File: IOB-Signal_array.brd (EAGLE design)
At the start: 104.1 x 106.7 mm, 49 parts

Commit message: Added missing values
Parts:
- C1X11, C1X12, C1X13, C1X14: value (none) -> 0.1uF
- IC1X11, IC1X12, IC1X13, IC1X14: value (none) -> 74HS139A
- R10X11, R10X12, R10X13, R10X14, R6X11, R6X12, R6X13, R6X14, R7X11, R7X12, R7X13, R7X14, R9X11, R9X12, R9X13, R9X14: value (none) -> 1k0
- R4X11, R4X12, R4X13, R4X14, R8X11, R8X12, R8X13, R8X14: value (none) -> 420R
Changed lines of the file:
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@@
 </autorouter>
 <elements>
-<element name="C1X11" library="SPCoast" package="0805-CAP" value="" x="54.61" y="17.526" rot="R270"/>
+<element name="C1X11" library="SPCoast" package="0805-CAP" value="0.1uF" x="54.61" y="17.526" rot="R270"/>
 <element name="CON1X11" library="SPCoast" package="RJ45-NO-SHIELD" value="" x="29.718" y="17.399" rot="R270"/>
 <element name="FID1X11" library="SPCoast" package="FIDUCIAL_1MM" value="" x="41.275" y="10.287"/>
 <element name="FID3X11" library="SPCoast" package="FIDUCIAL_1MM" value="" x="76.835" y="27.305"/>
-<element name="IC1X11" library="SPCoast" package="SO16" value="" x="60.833" y="17.399"/>
-<element name="R4X11" library="SPCoast" package="0805-RES" value="" x="50.8" y="15.494"/>
-<element name="R6X11" library="SPCoast" package="0805-RES" value="" x="46.99" y="14.224"/>
-<element name="R7X11" library="SPCoast" package="0805-RES" value="" x="46.99" y="16.764"/>
-<element name="R8X11" library="SPCoast" package="0805-RES" value="" x="50.8" y="20.574"/>
-<element name="R9X11" library="SPCoast" package="0805-RES" value="" x="46.99" y="19.304"/>
-<element name="R10X11" library="SPCoast" package="0805-RES" value="" x="46.99" y="21.844"/>
+<element name="IC1X11" library="SPCoast" package="SO16" value="74HS139A" x="60.833" y="17.399"/>
+<element name="R4X11" library="SPCoast" package="0805-RES" value="420R" x="50.8" y="15.494"/>
+<element name="R6X11" library="SPCoast" package="0805-RES" value="1k0" x="46.99" y="14.224"/>
+<element name="R7X11" library="SPCoast" package="0805-RES" value="1k0" x="46.99" y="16.764"/>
+<element name="R8X11" library="SPCoast" package="0805-RES" value="420R" x="50.8" y="20.574"/>
+<element name="R9X11" library="SPCoast" package="0805-RES" value="1k0" x="46.99" y="19.304"/>
+<element name="R10X11" library="SPCoast" package="0805-RES" value="1k0" x="46.99" y="21.844"/>
 <element name="U$1X11" library="SPCoast" package="IO4-IOB" value="" x="25.4" y="8.89"/>
-<element name="C1X12" library="SPCoast" package="0805-CAP" value="" x="54.61" y="37.846" rot="R270"/>
+<element name="C1X12" library="SPCoast" package="0805-CAP" value="0.1uF" x="54.61" y="37.846" rot="R270"/>
 <element name="CON1X12" library="SPCoast" package="RJ45-NO-SHIELD" value="" x="29.718" y="37.719" rot="R270"/>
 <element name="FID1X12" library="SPCoast" package="FIDUCIAL_1MM" value="" x="41.275" y="30.607"/>
 <element name="FID3X12" library="SPCoast" package="FIDUCIAL_1MM" value="" x="76.835" y="47.625"/>
-<element name="IC1X12" library="SPCoast" package="SO16" value="" x="60.833" y="37.719"/>
-<element name="R4X12" library="SPCoast" package="0805-RES" value="" x="50.8" y="35.814"/>
-<element name="R6X12" library="SPCoast" package="0805-RES" value="" x="46.99" y="34.544"/>
-<element name="R7X12" library="SPCoast" package="0805-RES" value="" x="46.99" y="37.084"/>
-<element name="R8X12" library="SPCoast" package="0805-RES" value="" x="50.8" y="40.894"/>
-<element name="R9X12" library="SPCoast" package="0805-RES" value="" x="46.99" y="39.624"/>
-<element name="R10X12" library="SPCoast" package="0805-RES" value="" x="46.99" y="42.164"/>
+<element name="IC1X12" library="SPCoast" package="SO16" value="74HS139A" x="60.833" y="37.719"/>
+<element name="R4X12" library="SPCoast" package="0805-RES" value="420R" x="50.8" y="35.814"/>
+<element name="R6X12" library="SPCoast" package="0805-RES" value="1k0" x="46.99" y="34.544"/>
+<element name="R7X12" library="SPCoast" package="0805-RES" value="1k0" x="46.99" y="37.084"/>
+<element name="R8X12" library="SPCoast" package="0805-RES" value="420R" x="50.8" y="40.894"/>
+<element name="R9X12" library="SPCoast" package="0805-RES" value="1k0" x="46.99" y="39.624"/>
+<element name="R10X12" library="SPCoast" package="0805-RES" value="1k0" x="46.99" y="42.164"/>
 <element name="U$1X12" library="SPCoast" package="IO4-IOB" value="" x="25.4" y="29.21"/>
-<element name="C1X13" library="SPCoast" package="0805-CAP" value="" x="54.61" y="58.166" rot="R270"/>
+<element name="C1X13" library="SPCoast" package="0805-CAP" value="0.1uF" x="54.61" y="58.166" rot="R270"/>
 <element name="CON1X13" library="SPCoast" package="RJ45-NO-SHIELD" value="" x="29.718" y="58.039" rot="R270"/>
 <element name="FID1X13" library="SPCoast" package="FIDUCIAL_1MM" value="" x="41.275" y="50.927"/>
 <element name="FID3X13" library="SPCoast" package="FIDUCIAL_1MM" value="" x="76.835" y="67.945"/>
-<element name="IC1X13" library="SPCoast" package="SO16" value="" x="60.833" y="58.039"/>
-<element name="R4X13" library="SPCoast" package="0805-RES" value="" x="50.8" y="56.134"/>
-<element name="R6X13" library="SPCoast" package="0805-RES" value="" x="46.99" y="54.864"/>
-<element name="R7X13" library="SPCoast" package="0805-RES" value="" x="46.99" y="57.404"/>
-<element name="R8X13" library="SPCoast" package="0805-RES" value="" x="50.8" y="61.214"/>
-<element name="R9X13" library="SPCoast" package="0805-RES" value="" x="46.99" y="59.944"/>
-<element name="R10X13" library="SPCoast" package="0805-RES" value="" x="46.99" y="62.484"/>
+<element name="IC1X13" library="SPCoast" package="SO16" value="74HS139A" x="60.833" y="58.039"/>
+<element name="R4X13" library="SPCoast" package="0805-RES" value="420R" x="50.8" y="56.134"/>
+<element name="R6X13" library="SPCoast" package="0805-RES" value="1k0" x="46.99" y="54.864"/>
+<element name="R7X13" library="SPCoast" package="0805-RES" value="1k0" x="46.99" y="57.404"/>
+<element name="R8X13" library="SPCoast" package="0805-RES" value="420R" x="50.8" y="61.214"/>
+<element name="R9X13" library="SPCoast" package="0805-RES" value="1k0" x="46.99" y="59.944"/>
+<element name="R10X13" library="SPCoast" package="0805-RES" value="1k0" x="46.99" y="62.484"/>
 <element name="U$1X13" library="SPCoast" package="IO4-IOB" value="" x="25.4" y="49.53"/>
-<element name="C1X14" library="SPCoast" package="0805-CAP" value="" x="54.61" y="78.486" rot="R270"/>
+<element name="C1X14" library="SPCoast" package="0805-CAP" value="0.1uF" x="54.61" y="78.486" rot="R270"/>
 <element name="CON1X14" library="SPCoast" package="RJ45-NO-SHIELD" value="" x="29.718" y="78.359" rot="R270"/>
 <element name="FID1X14" library="SPCoast" package="FIDUCIAL_1MM" value="" x="41.275" y="71.247"/>
 <element name="FID3X14" library="SPCoast" package="FIDUCIAL_1MM" value="" x="76.835" y="88.265"/>
-<element name="IC1X14" library="SPCoast" package="SO16" value="" x="60.833" y="78.359"/>
-<element name="R4X14" library="SPCoast" package="0805-RES" value="" x="50.8" y="76.454"/>
-<element name="R6X14" library="SPCoast" package="0805-RES" value="" x="46.99" y="75.184"/>
-<element name="R7X14" library="SPCoast" package="0805-RES" value="" x="46.99" y="77.724"/>
-<element name="R8X14" library="SPCoast" package="0805-RES" value="" x="50.8" y="81.534"/>
-<element name="R9X14" library="SPCoast" package="0805-RES" value="" x="46.99" y="80.264"/>
-<element name="R10X14" library="SPCoast" package="0805-RES" value="" x="46.99" y="82.804"/>
+<element name="IC1X14" library="SPCoast" package="SO16" value="74HS139A" x="60.833" y="78.359"/>
+<element name="R4X14" library="SPCoast" package="0805-RES" value="420R" x="50.8" y="76.454"/>
+<element name="R6X14" library="SPCoast" package="0805-RES" value="1k0" x="46.99" y="75.184"/>
+<element name="R7X14" library="SPCoast" package="0805-RES" value="1k0" x="46.99" y="77.724"/>
+<element name="R8X14" library="SPCoast" package="0805-RES" value="420R" x="50.8" y="81.534"/>
+<element name="R9X14" library="SPCoast" package="0805-RES" value="1k0" x="46.99" y="80.264"/>
+<element name="R10X14" library="SPCoast" package="0805-RES" value="1k0" x="46.99" y="82.804"/>
 <element name="U$1X14" library="SPCoast" package="IO4-IOB" value="" x="25.4" y="69.85"/>
 <element name="U$1X1" library="SPCoast" package="BOARD-DINRAIL-3.17IN-H4X-IOB" value="" x="0" y="0"/>

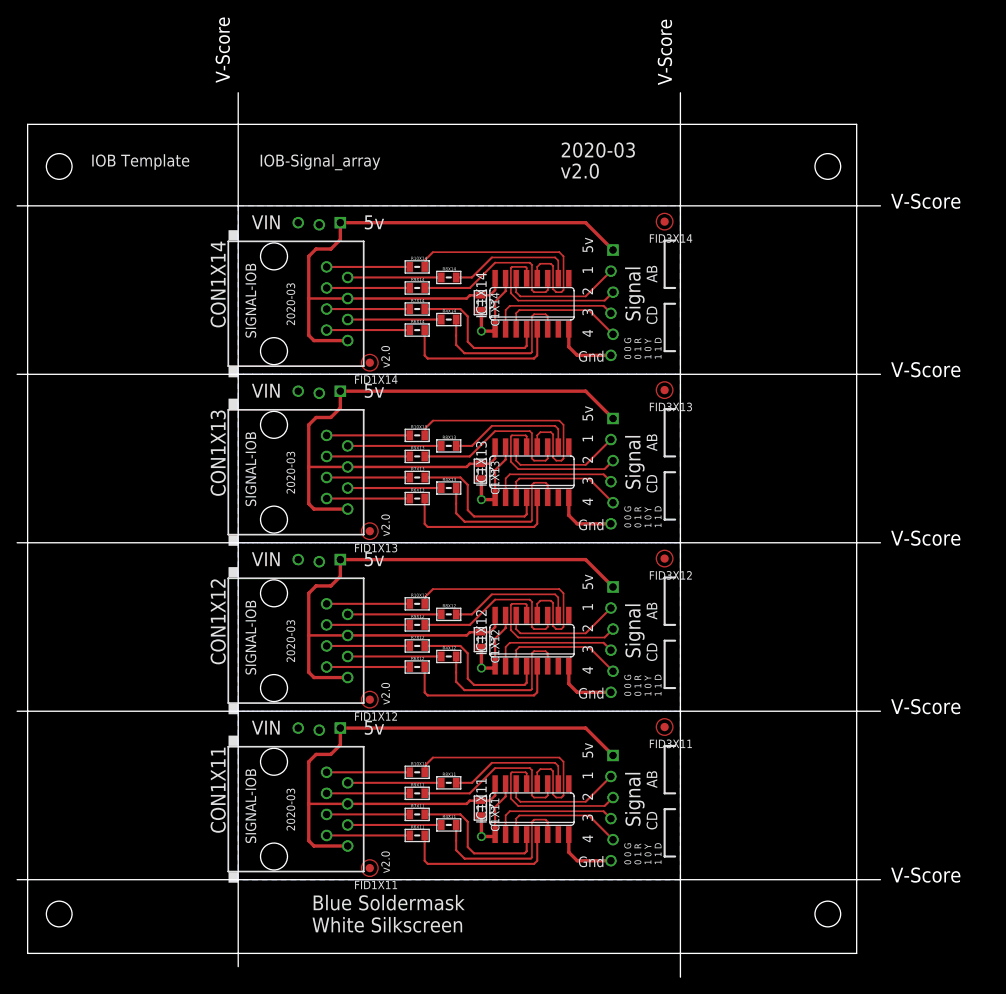
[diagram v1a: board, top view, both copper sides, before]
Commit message: normalized silkscreen layout across IOBs
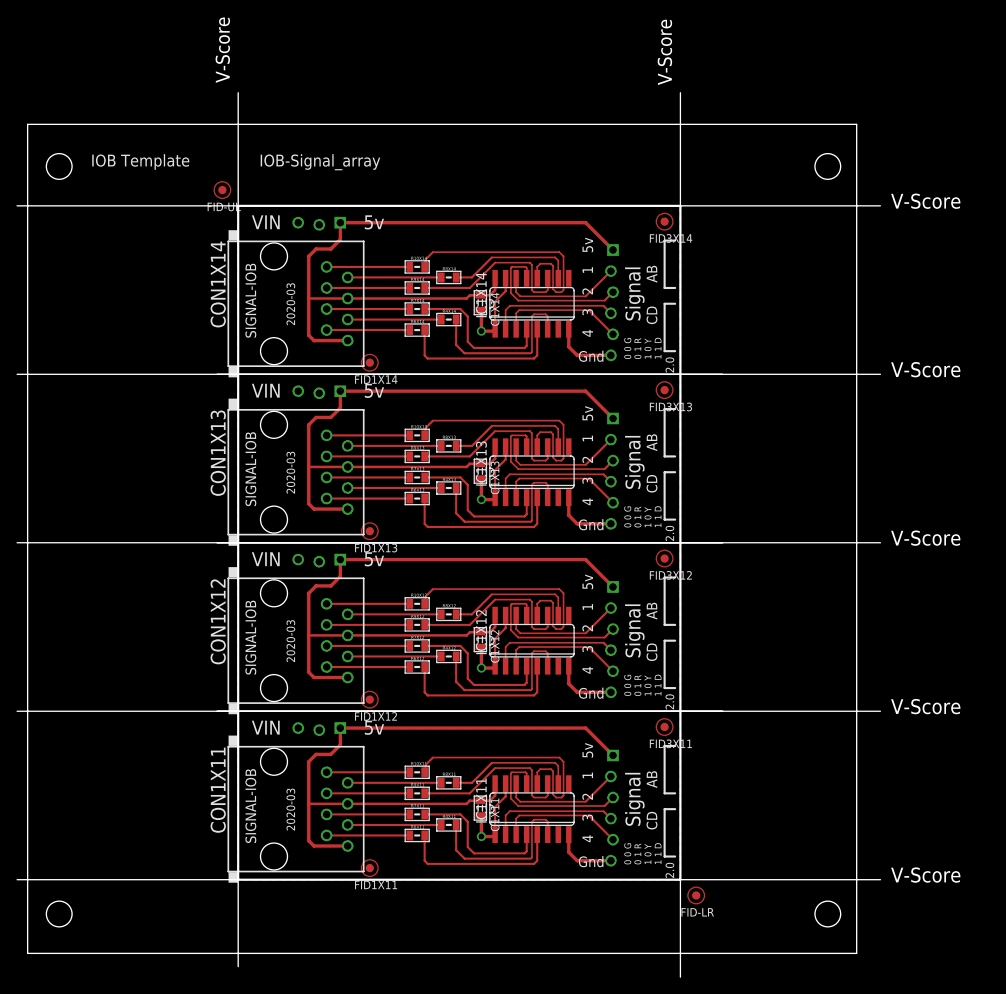
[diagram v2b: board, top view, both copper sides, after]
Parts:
- added FID-LR, FID-UL: FIDUCIAL, SPCoast:FIDUCIAL_1MM
- C1X11, C1X12, C1X13, C1X14: value 0.1uF -> 0.1UF
- CON1X11, CON1X12, CON1X13, CON1X14: value (none) -> RJ45
- FID1X11, FID1X12, FID1X13, FID1X14, FID3X11, FID3X12, FID3X13, FID3X14: value (none) -> FIDUCIAL
- R10X11, R10X12, R10X13, R10X14, R6X11, R6X12, R6X13, R6X14, R7X11, R7X12, R7X13, R7X14, R9X11, R9X12, R9X13, R9X14: value 1k0 -> 1K0
- U$1X11, U$1X12, U$1X13, U$1X14: value (none) -> CONNECTOR-IO4-IOBBARE
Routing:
- added copper zone on layer 1, net VCCX11
- added copper zone on layer 1, net VCCX12
- added copper zone on layer 1, net VCCX13
- added copper zone on layer 1, net VCCX14
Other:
- board text added: "2.0"
- board text added: "Blue Header"
- board text removed: "v2.0"

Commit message: bottom silk alignment
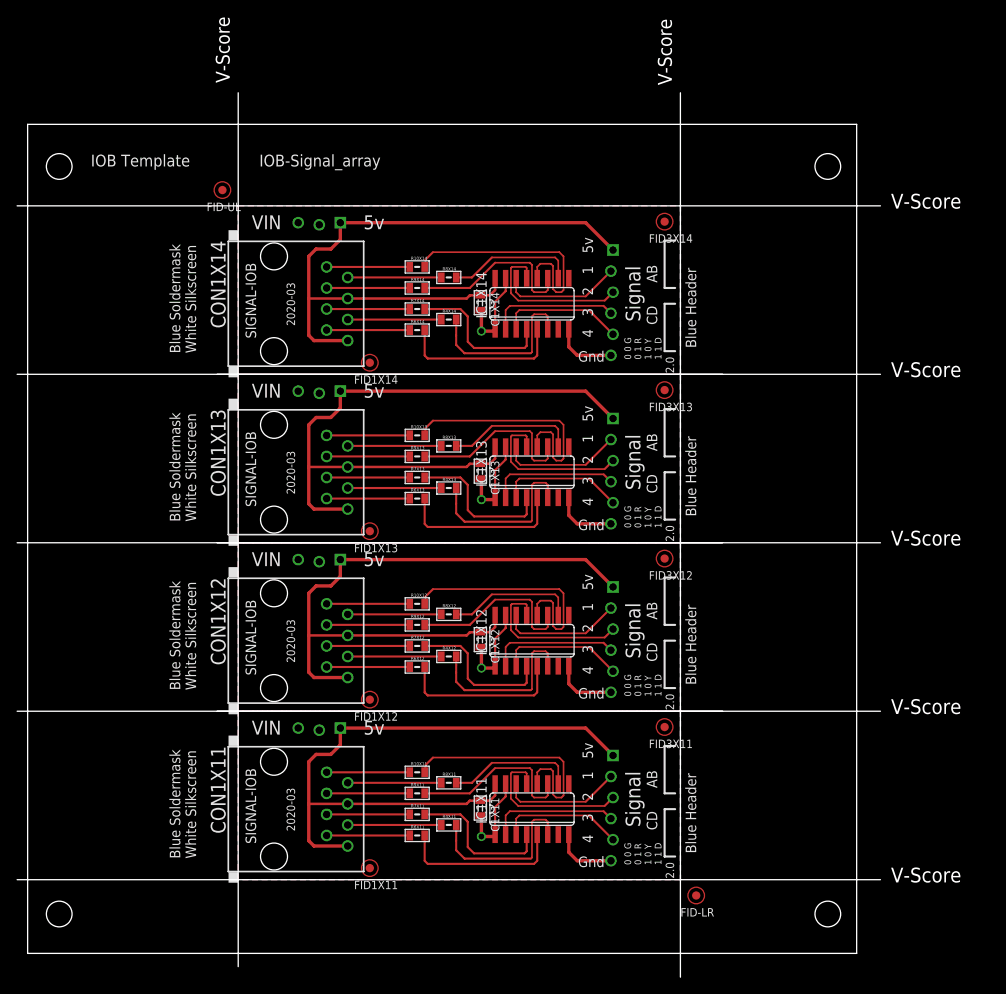
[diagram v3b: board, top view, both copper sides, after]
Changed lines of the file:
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@@
 <layer number="19" name="Unrouted" color="6" fill="1" visible="yes" active="yes"/>
 <layer number="20" name="Dimension" color="15" fill="1" visible="yes" active="yes"/>
-<layer number="21" name="tPlace" color="7" fill="1" visible="yes" active="yes"/>
+<layer number="21" name="tPlace" color="19" fill="1" visible="yes" active="yes"/>
 <layer number="22" name="bPlace" color="7" fill="1" visible="no" active="yes"/>
 <layer number="23" name="tOrigins" color="15" fill="1" visible="yes" active="yes"/>
@@
 <text x="75.946" y="19.939" size="1.27" layer="21" rot="R90">AB</text>
 <text x="75.946" y="14.859" size="1.27" layer="21" rot="R90">CD</text>
-<text x="20.32" y="11.43" size="1.27" layer="48" font="vector" ratio="10" rot="R90">Blue Soldermask
+<text x="20.32" y="11.43" size="1.27" layer="21" font="vector" ratio="10" rot="R90">Blue Soldermask
 White Silkscreen</text>
 <text x="32.258" y="14.732" size="1.016" layer="21" rot="R90">2020-03</text>
-<text x="80.645" y="12.065" size="1.27" layer="48" font="vector" ratio="10" rot="R90">Blue Header</text>
+<text x="80.645" y="12.065" size="1.27" layer="21" font="vector" ratio="10" rot="R90">Blue Header</text>
 <text x="54.102" y="19.431" size="0.8128" layer="125" font="vector">C1</text>
 <text x="22.098" y="25.019" size="1.016" layer="125" font="vector" rot="R270">CON1</text>
@@
 <text x="75.946" y="40.259" size="1.27" layer="21" rot="R90">AB</text>
 <text x="75.946" y="35.179" size="1.27" layer="21" rot="R90">CD</text>
-<text x="20.32" y="31.75" size="1.27" layer="48" font="vector" ratio="10" rot="R90">Blue Soldermask
+<text x="20.32" y="31.75" size="1.27" layer="21" font="vector" ratio="10" rot="R90">Blue Soldermask
 White Silkscreen</text>
 <text x="32.258" y="35.052" size="1.016" layer="21" rot="R90">2020-03</text>
-<text x="80.645" y="32.385" size="1.27" layer="48" font="vector" ratio="10" rot="R90">Blue Header</text>
+<text x="80.645" y="32.385" size="1.27" layer="21" font="vector" ratio="10" rot="R90">Blue Header</text>
 <text x="54.102" y="39.751" size="0.8128" layer="125" font="vector">C1</text>
 <text x="22.098" y="45.339" size="1.016" layer="125" font="vector" rot="R270">CON1</text>
@@
 <text x="75.946" y="60.579" size="1.27" layer="21" rot="R90">AB</text>
 <text x="75.946" y="55.499" size="1.27" layer="21" rot="R90">CD</text>
-<text x="20.32" y="52.07" size="1.27" layer="48" font="vector" ratio="10" rot="R90">Blue Soldermask
+<text x="20.32" y="52.07" size="1.27" layer="21" font="vector" ratio="10" rot="R90">Blue Soldermask
 White Silkscreen</text>
 <text x="32.258" y="55.372" size="1.016" layer="21" rot="R90">2020-03</text>
-<text x="80.645" y="52.705" size="1.27" layer="48" font="vector" ratio="10" rot="R90">Blue Header</text>
+<text x="80.645" y="52.705" size="1.27" layer="21" font="vector" ratio="10" rot="R90">Blue Header</text>
 <text x="54.102" y="60.071" size="0.8128" layer="125" font="vector">C1</text>
 <text x="22.098" y="65.659" size="1.016" layer="125" font="vector" rot="R270">CON1</text>
@@
 <text x="46.228" y="63.3095" size="0.4064" layer="125" font="vector">R10</text>
 <wire x1="22.86" y1="69.85" x2="83.82" y2="69.85" width="0" layer="46"/>
-<wire x1="25.4" y1="8.89" x2="78.74" y2="8.89" width="0.254" layer="20"/>
-<wire x1="78.74" y1="8.89" x2="78.74" y2="90.17" width="0.254" layer="20"/>
-<wire x1="78.74" y1="90.17" x2="25.4" y2="90.17" width="0.254" layer="20"/>
-<wire x1="25.4" y1="90.17" x2="25.4" y2="8.89" width="0.254" layer="20"/>
 <wire x1="78.74" y1="69.85" x2="78.74" y2="90.17" width="0" layer="101"/>
 <wire x1="78.74" y1="90.17" x2="25.4" y2="90.17" width="0" layer="101"/>
@@
 <text x="75.946" y="80.899" size="1.27" layer="21" rot="R90">AB</text>
 <text x="75.946" y="75.819" size="1.27" layer="21" rot="R90">CD</text>
-<text x="20.32" y="72.39" size="1.27" layer="48" font="vector" ratio="10" rot="R90">Blue Soldermask
+<text x="20.32" y="72.39" size="1.27" layer="21" font="vector" ratio="10" rot="R90">Blue Soldermask
 White Silkscreen</text>
 <text x="32.258" y="75.692" size="1.016" layer="21" rot="R90">2020-03</text>
-<text x="80.645" y="73.025" size="1.27" layer="48" font="vector" ratio="10" rot="R90">Blue Header</text>
+<text x="80.645" y="73.025" size="1.27" layer="21" font="vector" ratio="10" rot="R90">Blue Header</text>
 <text x="54.102" y="80.391" size="0.8128" layer="125" font="vector">C1</text>
 <text x="22.098" y="85.979" size="1.016" layer="125" font="vector" rot="R270">CON1</text>
